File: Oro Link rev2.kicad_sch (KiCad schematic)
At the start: 0 parts

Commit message: begin refactor for rev3
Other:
- sheet External Ethernet: file external-ethernet.kicad_sch -> ethernet.kicad_sch
- sheet Microcontroller ports: added none; removed ETH_ECRSDV, ETH_EMDC, ETH_EREFCLK, ETH_ERXD0, ETH_ERXD1, ETH_ERXERR, ETH_ETXD0, ETH_ETXD1, ETH_ETXEN, ETH_INT, ETH_MDIO, ETH_~{RST}, EXTETH_~{CS}
- sheet System Ethernet: file system-ethernet.kicad_sch -> ethernet.kicad_sch
- sheet System Ethernet ports: added SCK, SDI, SDO, ~{CS}, ~{INT}; removed CRSDV, INT, MDC, MDIO, REFCLK, RXD0, RXD1, RXERR, TXD0, TXD1, TXEN

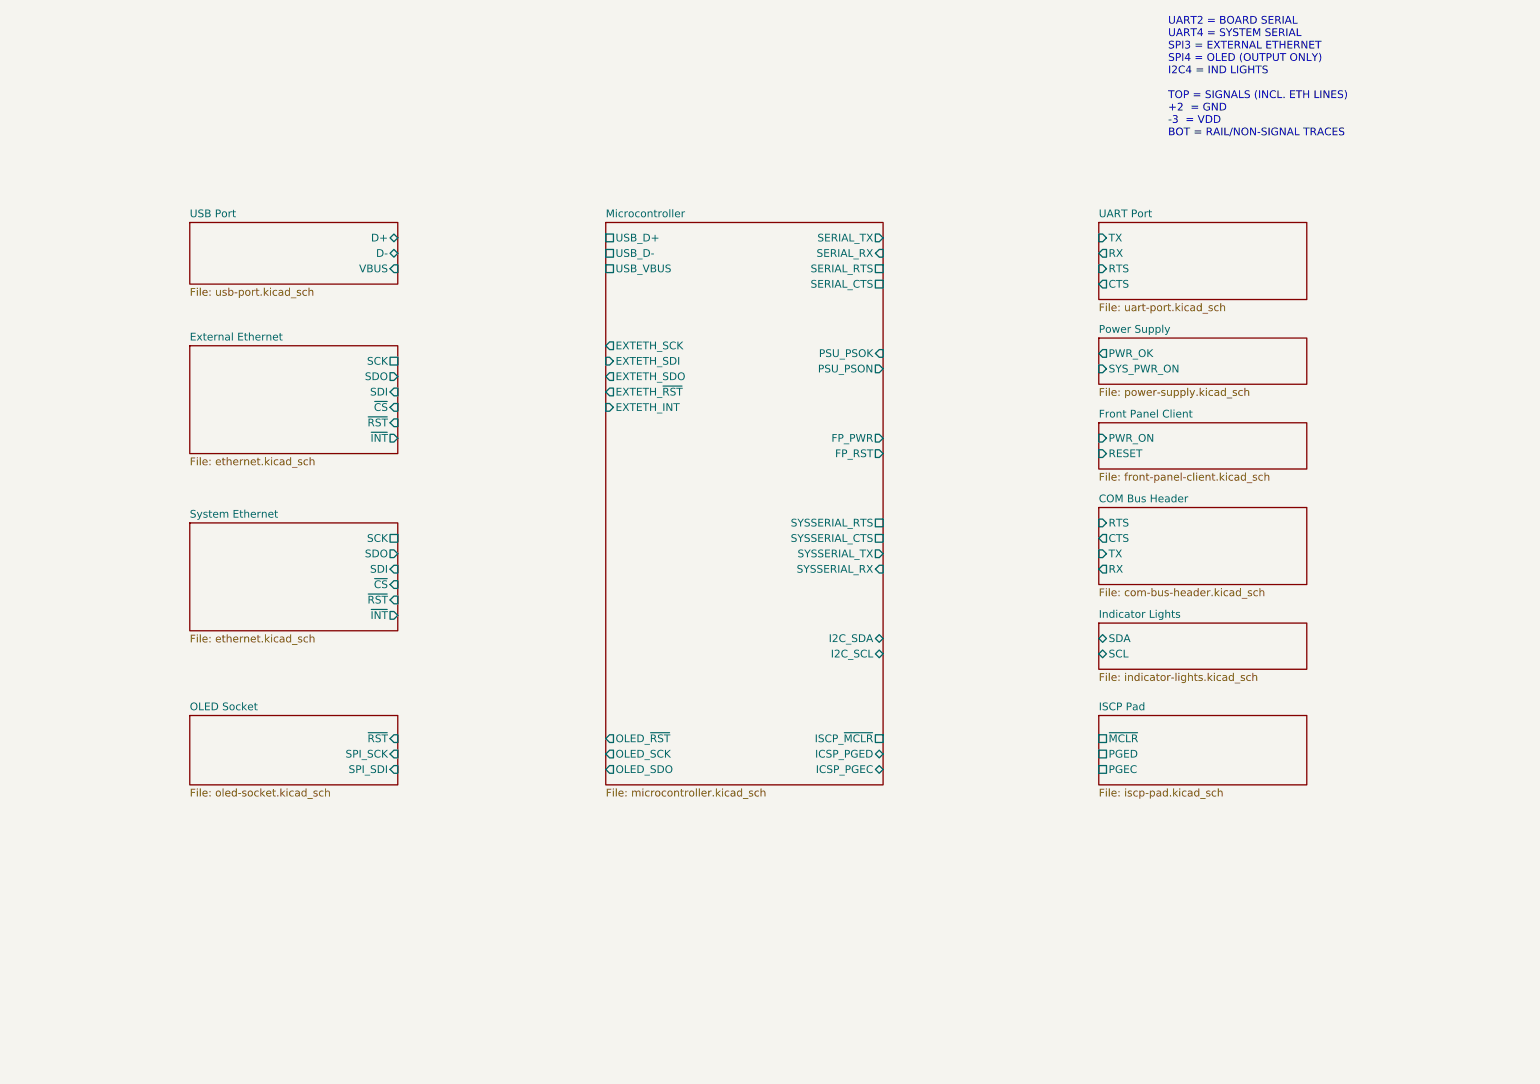
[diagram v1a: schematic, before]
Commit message: fully move to new MCU configuration
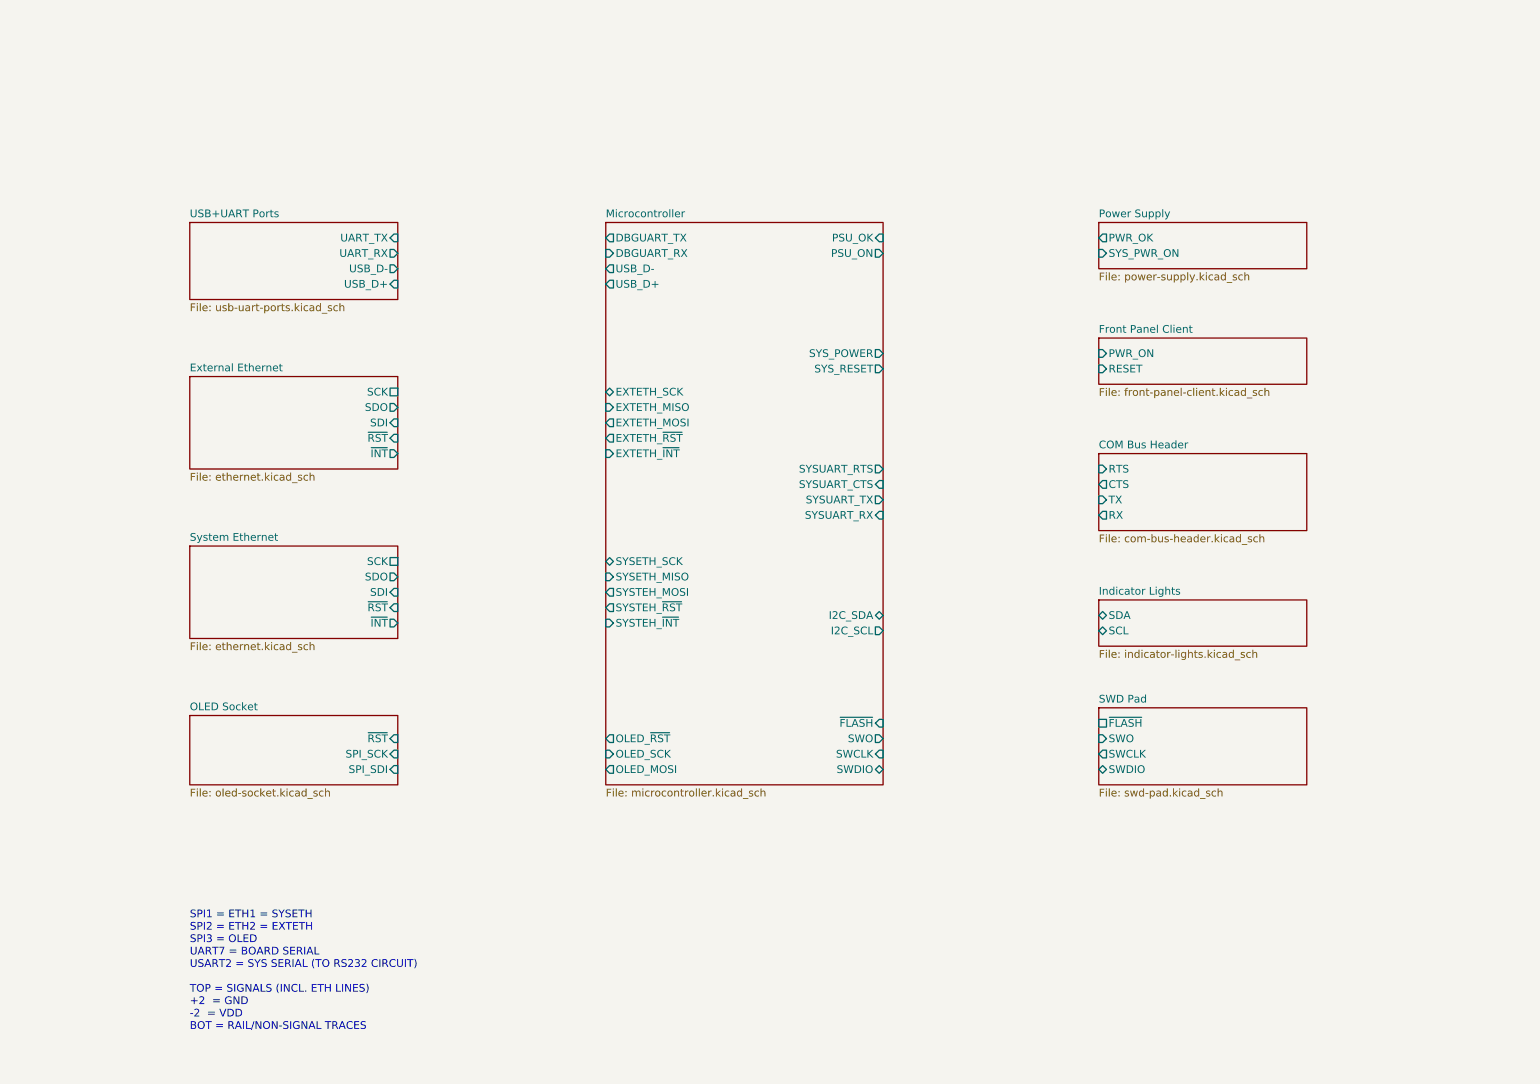
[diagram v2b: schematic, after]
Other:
- sheet ISCP Pad renamed SWD Pad
- sheet UART Port renamed USB+UART Ports
- removed sheet USB Port
- sheet External Ethernet ports: added none; removed ~{CS}
- sheet Microcontroller ports: added DBGUART_RX, DBGUART_TX, EXTETH_MISO, EXTETH_MOSI, EXTETH_~{INT}, OLED_MOSI, PSU_OK, PSU_ON, SWCLK, SWDIO, SWO, SYSETH_MISO, SYSETH_SCK, SYSTEH_MOSI, SYSTEH_~{INT}, SYSTEH_~{RST}, SYSUART_CTS, SYSUART_RTS, SYSUART_RX, SYSUART_TX, SYS_POWER, SYS_RESET, ~{FLASH}; removed EXTETH_INT, EXTETH_SDI, EXTETH_SDO, FP_PWR, FP_RST, ICSP_PGEC, ICSP_PGED, ISCP_~{MCLR}, OLED_SDO, PSU_PSOK, PSU_PSON, SERIAL_CTS, SERIAL_RTS, SERIAL_RX, SERIAL_TX, SYSSERIAL_CTS, SYSSERIAL_RTS, SYSSERIAL_RX, SYSSERIAL_TX, USB_VBUS
- sheet SWD Pad: file iscp-pad.kicad_sch -> swd-pad.kicad_sch
- sheet SWD Pad ports: added SWCLK, SWDIO, SWO, ~{FLASH}; removed PGEC, PGED, ~{MCLR}
- sheet System Ethernet ports: added none; removed ~{CS}
- sheet USB+UART Ports: file uart-port.kicad_sch -> usb-uart-ports.kicad_sch
- sheet USB+UART Ports ports: added UART_RX, UART_TX, USB_D+, USB_D-; removed CTS, RTS, RX, TX
- note added: "SPI1 = ETH1 = SYSETH SPI2 = ETH2 = EXTETH SPI3 = OLED UART7 = BOARD SERIAL USART2 = SYS SERIAL (TO RS232 CIRCUIT) TOP = SIGNALS (INCL. ETH LINES) +2 = GND -2 = VDD BOT = RAIL/NON-SIGNAL TRACES"
- note removed: "UART2 = BOARD SERIAL UART4 = SYSTEM SERIAL SPI3 = EXTERNAL ETHERNET SPI4 = OLED (OUTPUT ONLY) I2C4 = IND LIGHTS TOP = SIGNALS (INCL. ETH LINES) +2 = GND -3 = VDD BOT = RAIL/NON-SIGNAL TRACES"

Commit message: first few boards laid out
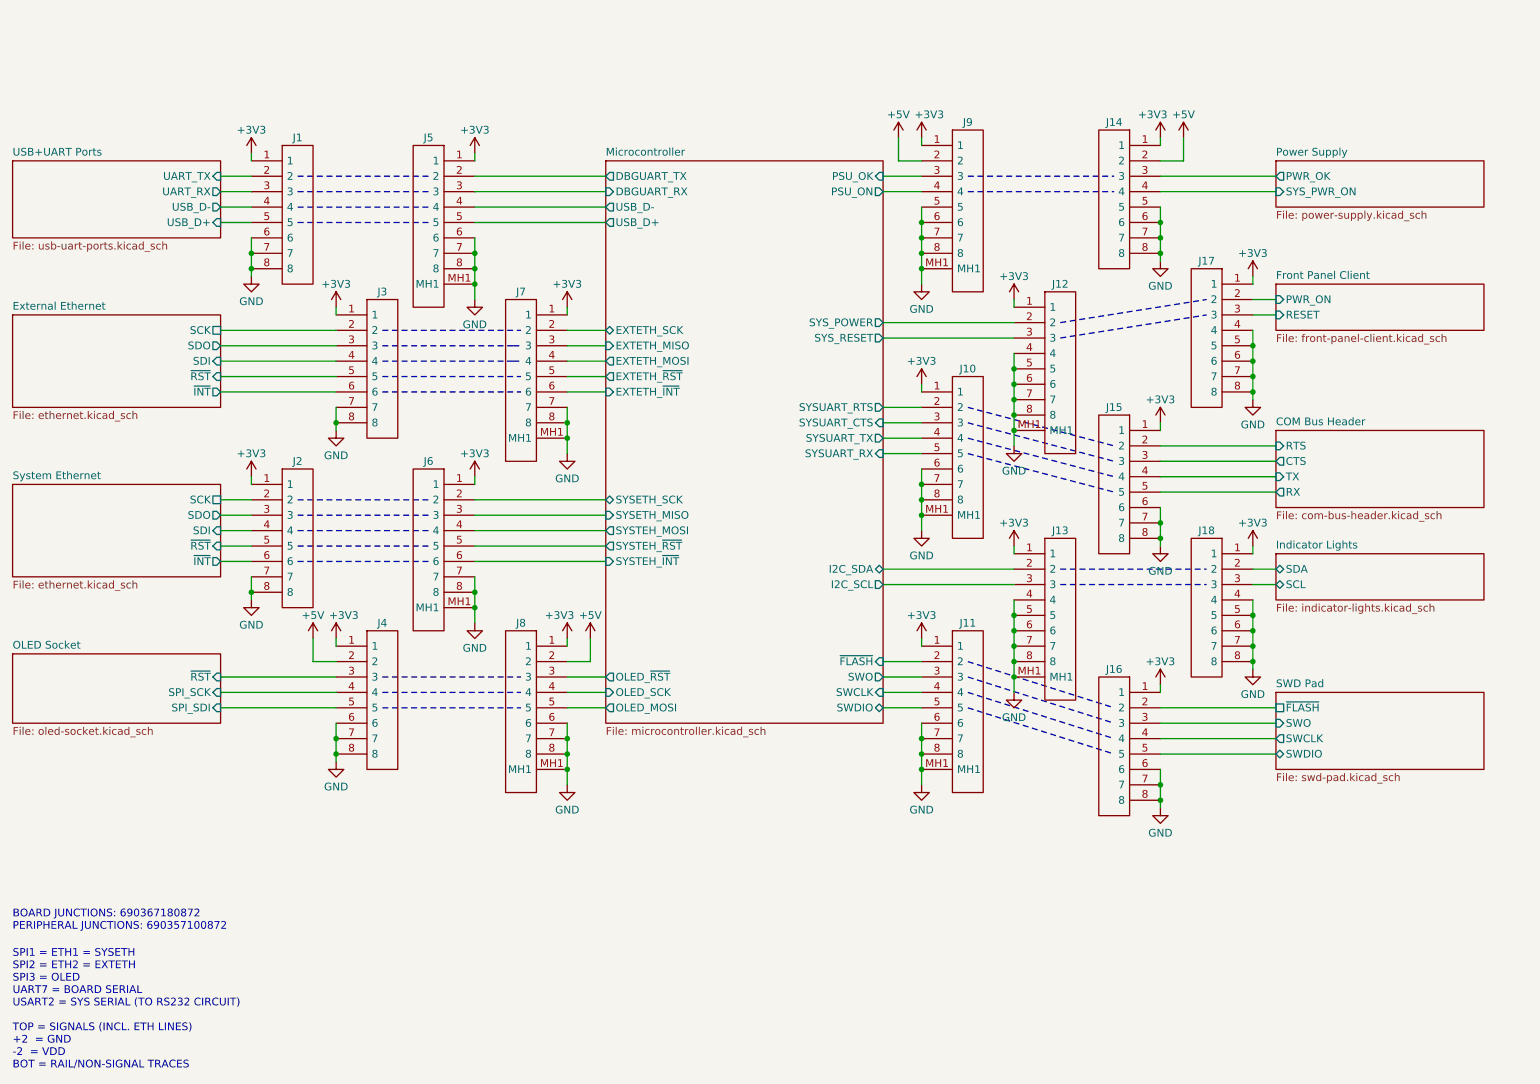
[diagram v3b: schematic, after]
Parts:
- added J1, J14, J15, J16, J17, J18, J2, J3, J4: 690357100872, Oro Footprints:690357100872, symbol Oro:690357100872
- added J10, J11, J12, J13, J5, J6, J7, J8, J9: 690367180872, 690367180872, symbol SamacSys_Parts:690367180872
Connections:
- net COM Bus Header/CTS: now also J15.3
- net COM Bus Header/RTS: now also J15.2
- net COM Bus Header/RX: now also J15.5
- net COM Bus Header/TX: now also J15.4
- net External Ethernet/SCK: now also J3.2
- net External Ethernet/SDI: now also J3.4
- net External Ethernet/SDO: now also J3.3
- net External Ethernet/~{INT}: now also J3.6
- net External Ethernet/~{RST}: now also J3.5
- net Front Panel Client/PWR_ON: now also J17.2
- net Front Panel Client/RESET: now also J17.3
- net Indicator Lights/SCL: now also J18.3
- net Indicator Lights/SDA: now also J18.2
- net Microcontroller/DBGUART_RX: now also J5.3
- net Microcontroller/DBGUART_TX: now also J5.2
- net Microcontroller/EXTETH_MISO: now also J7.3
- net Microcontroller/EXTETH_MOSI: now also J7.4
- net Microcontroller/EXTETH_SCK: now also J7.2
- net Microcontroller/EXTETH_~{INT}: now also J7.6
- net Microcontroller/EXTETH_~{RST}: now also J7.5
- net Microcontroller/I2C_SCL: now also J13.3
- net Microcontroller/I2C_SDA: now also J13.2
- net Microcontroller/OLED_MOSI: now also J8.5
- net Microcontroller/OLED_SCK: now also J8.4
- net Microcontroller/OLED_~{RST}: now also J8.3
- net Microcontroller/PSU_OK: now also J9.3
- net Microcontroller/PSU_ON: now also J9.4
- net Microcontroller/SWCLK: now also J11.4
- net Microcontroller/SWDIO: now also J11.5
- net Microcontroller/SWO: now also J11.3
- net Microcontroller/SYSETH_MISO: now also J6.3
- net Microcontroller/SYSETH_SCK: now also J6.2
- net Microcontroller/SYSTEH_MOSI: now also J6.4
- net Microcontroller/SYSTEH_~{INT}: now also J6.6
- net Microcontroller/SYSTEH_~{RST}: now also J6.5
- net Microcontroller/SYSUART_CTS: now also J10.3
- net Microcontroller/SYSUART_RTS: now also J10.2
- net Microcontroller/SYSUART_RX: now also J10.5
- net Microcontroller/SYSUART_TX: now also J10.4
- net Microcontroller/SYS_POWER: now also J12.2
- net Microcontroller/SYS_RESET: now also J12.3
- net Microcontroller/USB_D+: now also J5.5
- net Microcontroller/USB_D-: now also J5.4
- net Microcontroller/~{FLASH}: now also J11.2
- net OLED Socket/SPI_SCK: now also J4.4
- net OLED Socket/SPI_SDI: now also J4.5
- net OLED Socket/~{RST}: now also J4.3
- net Power Supply/PWR_OK: now also J14.3
- net Power Supply/SYS_PWR_ON: now also J14.4
- net SWD Pad/SWCLK: now also J16.4
- net SWD Pad/SWDIO: now also J16.5
- net SWD Pad/SWO: now also J16.3
- net SWD Pad/~{FLASH}: now also J16.2
- net System Ethernet/SCK: now also J2.2
- net System Ethernet/SDI: now also J2.4
- net System Ethernet/SDO: now also J2.3
- net System Ethernet/~{INT}: now also J2.6
- net System Ethernet/~{RST}: now also J2.5
- net USB+UART Ports/UART_RX: now also J1.3
- net USB+UART Ports/UART_TX: now also J1.2
- net USB+UART Ports/USB_D+: now also J1.5
- net USB+UART Ports/USB_D-: now also J1.4
- new net +3V3: J1.1, J10.1, J11.1, J12.1, J13.1, J14.1, J15.1, J16.1, J17.1, J18.1, J2.1, J3.1, J4.1, J5.1, J6.1, J7.1, J8.1, J9.1
- new net +5V: J14.2, J4.2, J8.2, J9.2
- new net GND: J1.6, J1.7, J1.8, J10.6, J10.7, J10.8, J10.MH1, J11.6, J11.7, J11.8, J11.MH1, J12.4, J12.5, J12.6, J12.7, J12.8, J12.MH1, J13.4, J13.5, J13.6, J13.7, J13.8, J13.MH1, J14.5, J14.6, J14.7, J14.8, J15.6, J15.7, J15.8, J16.6, J16.7, J16.8, J17.4, J17.5, J17.6, J17.7, J17.8, J18.4, J18.5, J18.6, J18.7, J18.8, J2.7, J2.8, J3.7, J3.8, J4.6, J4.7, J4.8, J5.6, J5.7, J5.8, J5.MH1, J6.7, J6.8, J6.MH1, J7.7, J7.8, J7.MH1, J8.6, J8.7, J8.8, J8.MH1, J9.5, J9.6, J9.7, J9.8, J9.MH1
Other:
- note added: "BOARD JUNCTIONS: 690367180872 PERIPHERAL JUNCTIONS: 690357100872"

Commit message: initial board layout
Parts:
- removed J1, J14, J15, J16, J17, J18, J2, J3, J4: 690357100872, Oro Footprints:690357100872, symbol Oro:690357100872
- removed J10, J11, J12, J13, J5, J6, J7, J8, J9: 690367180872, 690367180872, symbol SamacSys_Parts:690367180872

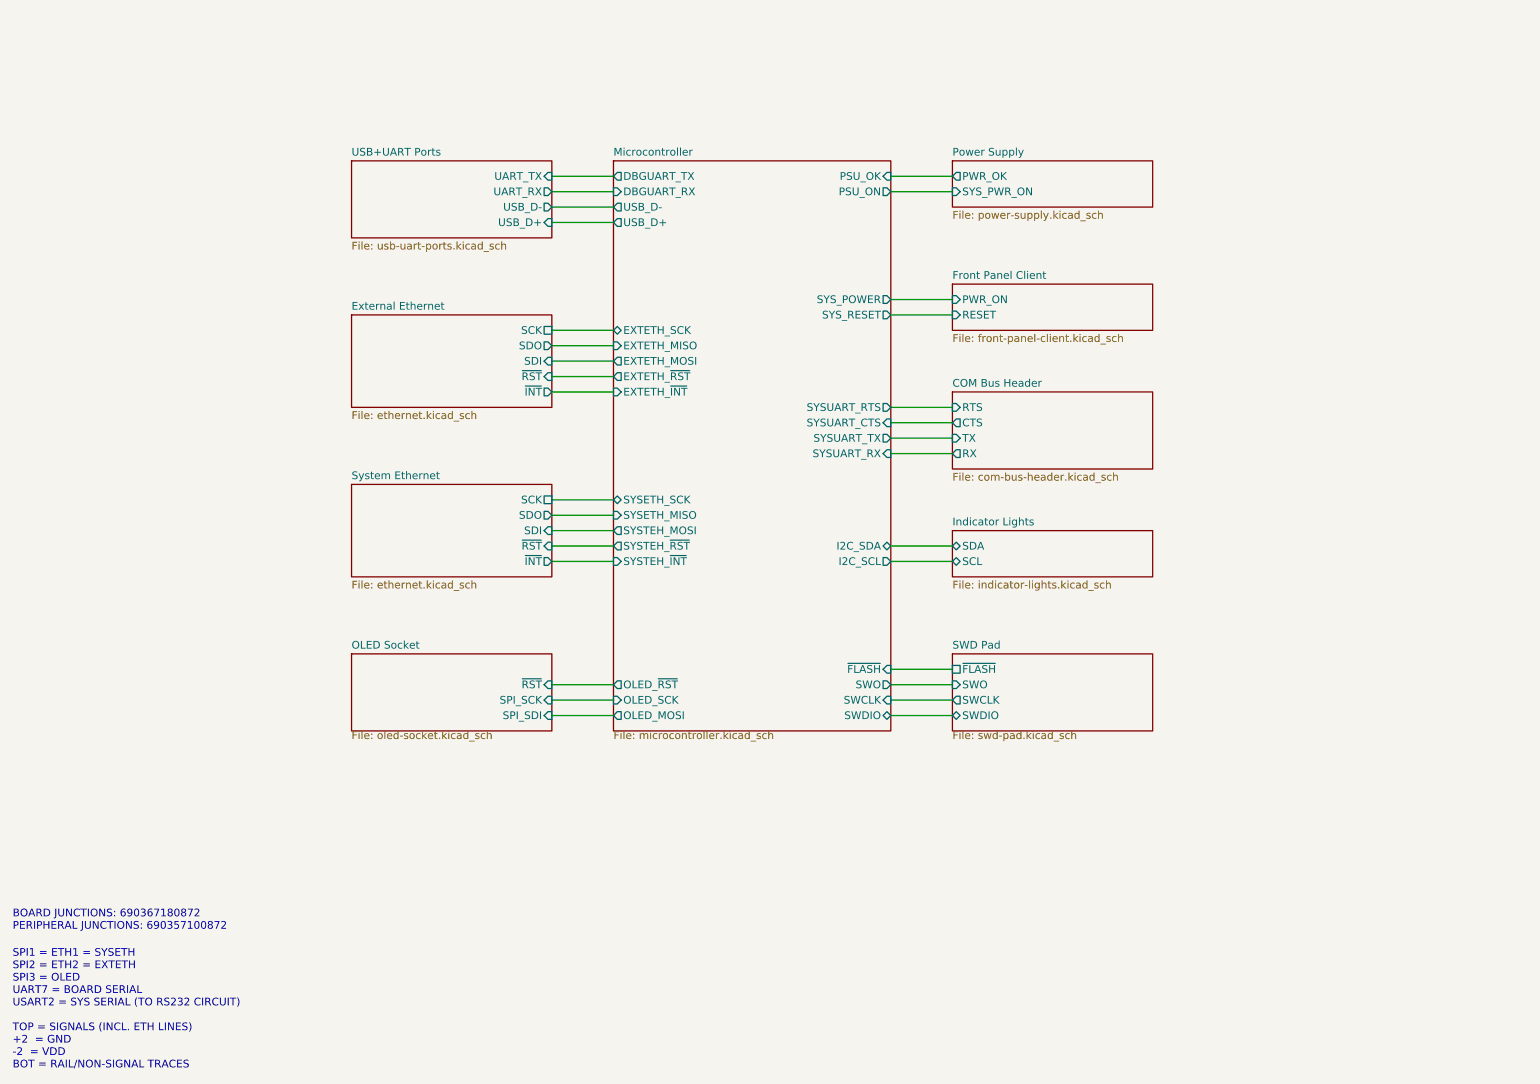
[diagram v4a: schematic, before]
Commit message: initial component layout
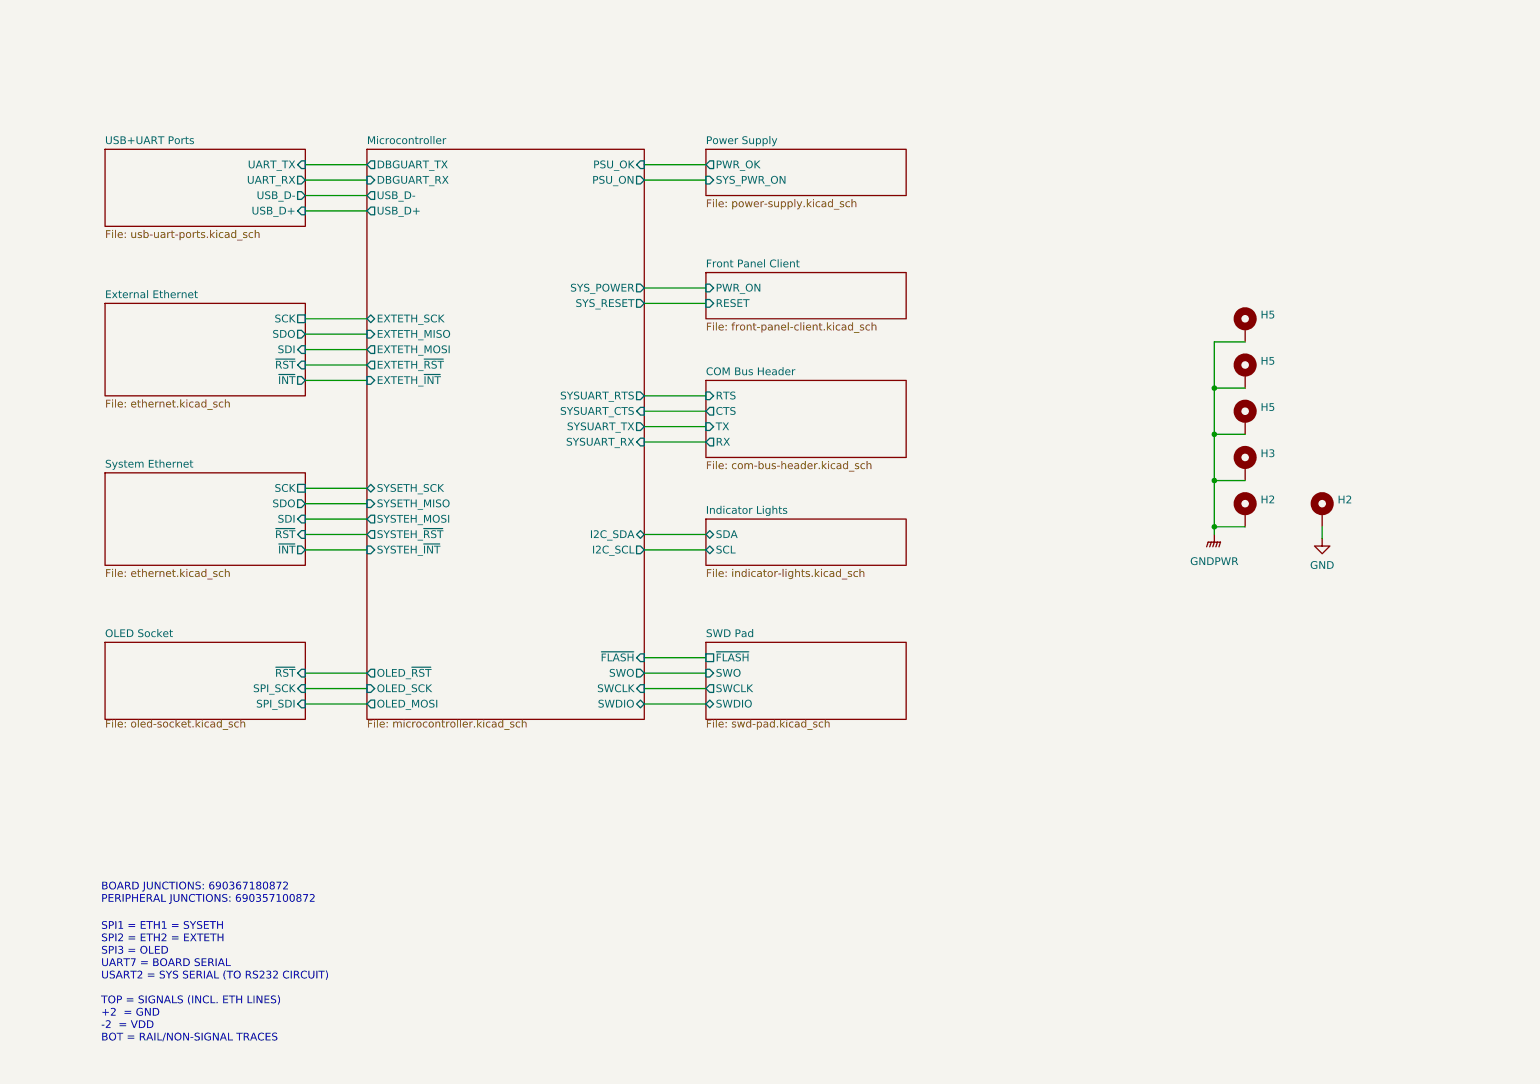
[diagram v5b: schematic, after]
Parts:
- added H2 (x2), H3, H5 (x3): MountingHole_Pad, MountingHole:MountingHole_3.2mm_M3_Pad_Via, symbol Mechanical:MountingHole_Pad
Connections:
- new net GND: H2.1
- new net GNDPWR: H2.1, H3.1, H5.1, H5.1, H5.1
